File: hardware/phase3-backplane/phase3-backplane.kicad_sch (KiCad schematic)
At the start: 29 parts, among them J1 MANAGER, J10 SLOT0 PWR, J11 SLOT1 PWR, J12 SLOT2 PWR, J13 SLOT3 PWR, J14 SLOT4 PWR, J15 SLOT5 PWR, J16 SLOT6 PWR, J17 SLOT7 PWR, J2 E-STOP NC (jumper if absent), J20 SLOT0 SIG, J21 SLOT1 SIG, J22 SLOT2 SIG, J23 SLOT3 SIG, J24 SLOT4 SIG, J25 SLOT5 SIG, J26 SLOT6 SIG, J27 SLOT7 SIG, J30 VBUS+ LUG M6, J31 RETURN LUG M6, U1 INA228

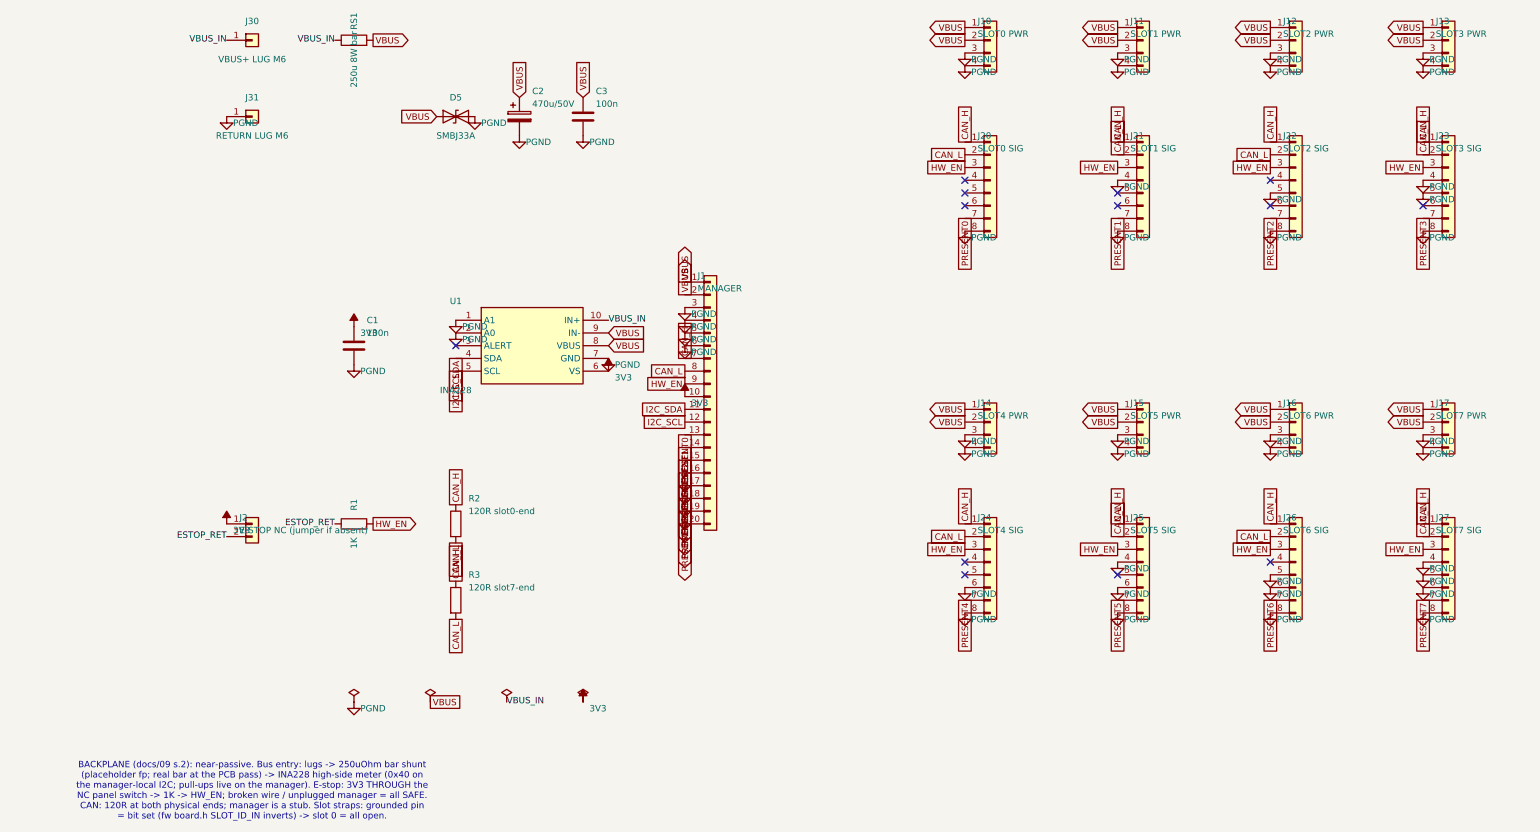
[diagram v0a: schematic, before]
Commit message: Apply China-sourcing engineering changes across all boards + mechanical frame
All datasheet-verified before application (details hardware/SOURCING.md sF):
- TMUX1101 -> TS5A3166DBVR (LCSC availability; ts5a3166.pdf: pin POSITIONS
  identical - 1=NO 2=COM 3=GND 4=IN 5=V+; VIH 2.4V ok from 3.3V GPIO)
- TLV7011 DBVR -> DCKR: tlv7022.pdf shows DBV/DCK share one pinout, so
  footprint-only (SOT-353_SC-70-5); SOT-23-5 stock in China is nearly gone
- crystal load caps 10p -> 18p, both phases (CL=12pF China crystals; the
  HANDOVER-blessed alternative to hunting CL=8pF parts)
- Phase-1 inductor -> MWSA1707S-100MT (JLCPCB-verified 16.5A Isat/10.5A
  Irms vs 12A/8A required); value strings now dual-source Sunlord/Coilcraft
- module slot power + P2 output -> XT60PW-M (2-pin), backplane slots ->
  XT60PW-F; bus shunt -> 2x BVS-M-R0005 parallel (the exact-net checker
  caught RS1/RS2 placed one pin-span apart merging VBUS_IN into VBUS)
- 470u bulk -> THT radial D10; output MLCCs 22u -> 10u/50V X7S; buzzer ->
  MLT-8530 (fp placeholder)
All four checker chains green: 137/173/30/80 components.

hardware/MECHANICAL.md (frozen): 30mm slot pitch, P2 130x90 4-layer,
backplane ~330x100 2-layer 2oz, manager 100x80; cost-first stackup (1oz
outer + solder-reinforced bus, 2oz only if the thermal soak demands it);
inductor footprint = SUPERSET pattern accepting Sunlord 1707 AND Coilcraft
XAL1510 so the A/B pair is a pure part swap.

HANDOVER: sub-0.5V mV-accurate output DEFERRED to a future dedicated
linear post-regulator module (user decision 2026-07-18); buck floors
documented (P2 0.7V @30V bus, P1 0.5V).

Co-Authored-By: Claude Fable 5 <noreply@anthropic.com>
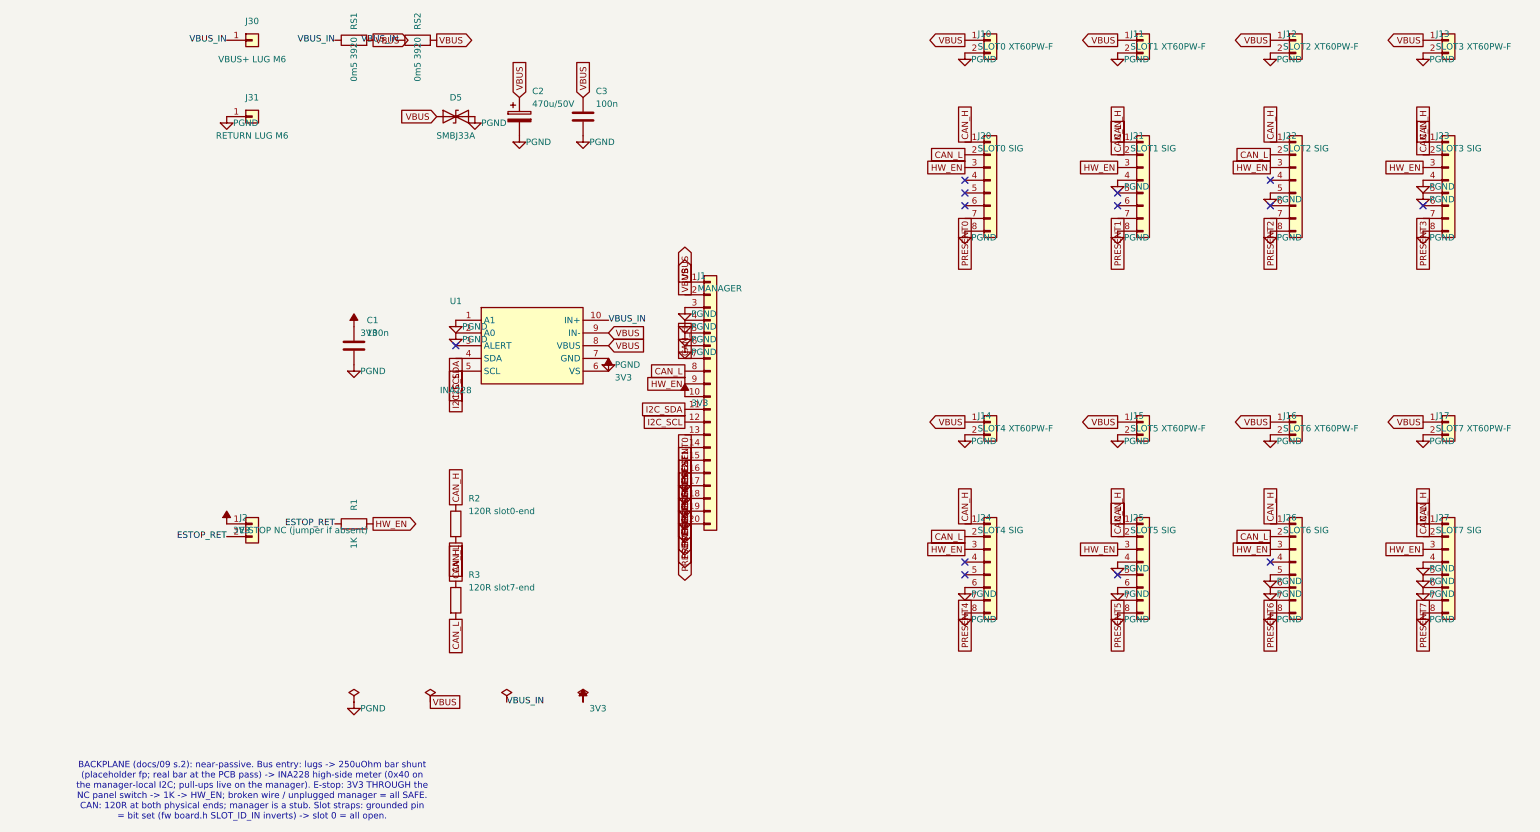
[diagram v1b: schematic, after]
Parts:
- removed J10: SLOT0 PWR, Connector_PinHeader_2.54mm:PinHeader_1x04_P2.54mm_Vertical, symbol Connector_Generic:Conn_01x04
- removed J11: SLOT1 PWR, Connector_PinHeader_2.54mm:PinHeader_1x04_P2.54mm_Vertical, symbol Connector_Generic:Conn_01x04
- removed J12: SLOT2 PWR, Connector_PinHeader_2.54mm:PinHeader_1x04_P2.54mm_Vertical, symbol Connector_Generic:Conn_01x04
- removed J13: SLOT3 PWR, Connector_PinHeader_2.54mm:PinHeader_1x04_P2.54mm_Vertical, symbol Connector_Generic:Conn_01x04
- removed J14: SLOT4 PWR, Connector_PinHeader_2.54mm:PinHeader_1x04_P2.54mm_Vertical, symbol Connector_Generic:Conn_01x04
- removed J15: SLOT5 PWR, Connector_PinHeader_2.54mm:PinHeader_1x04_P2.54mm_Vertical, symbol Connector_Generic:Conn_01x04
- removed J16: SLOT6 PWR, Connector_PinHeader_2.54mm:PinHeader_1x04_P2.54mm_Vertical, symbol Connector_Generic:Conn_01x04
- removed J17: SLOT7 PWR, Connector_PinHeader_2.54mm:PinHeader_1x04_P2.54mm_Vertical, symbol Connector_Generic:Conn_01x04
- added J10: SLOT0 XT60PW-F, Connector_PinHeader_2.54mm:PinHeader_1x02_P2.54mm_Vertical, symbol Connector_Generic:Conn_01x02
- added J11: SLOT1 XT60PW-F, Connector_PinHeader_2.54mm:PinHeader_1x02_P2.54mm_Vertical, symbol Connector_Generic:Conn_01x02
- added J12: SLOT2 XT60PW-F, Connector_PinHeader_2.54mm:PinHeader_1x02_P2.54mm_Vertical, symbol Connector_Generic:Conn_01x02
- added J13: SLOT3 XT60PW-F, Connector_PinHeader_2.54mm:PinHeader_1x02_P2.54mm_Vertical, symbol Connector_Generic:Conn_01x02
- added J14: SLOT4 XT60PW-F, Connector_PinHeader_2.54mm:PinHeader_1x02_P2.54mm_Vertical, symbol Connector_Generic:Conn_01x02
- added J15: SLOT5 XT60PW-F, Connector_PinHeader_2.54mm:PinHeader_1x02_P2.54mm_Vertical, symbol Connector_Generic:Conn_01x02
- added J16: SLOT6 XT60PW-F, Connector_PinHeader_2.54mm:PinHeader_1x02_P2.54mm_Vertical, symbol Connector_Generic:Conn_01x02
- added J17: SLOT7 XT60PW-F, Connector_PinHeader_2.54mm:PinHeader_1x02_P2.54mm_Vertical, symbol Connector_Generic:Conn_01x02
- added RS2: 0m5 3920, Resistor_SMD:R_2512_6332Metric, symbol Device:R
- RS1: value 250u 8W bar -> 0m5 3920
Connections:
- net PGND: now also J10.2 (Pin_2), J11.2 (Pin_2), J12.2 (Pin_2), J13.2 (Pin_2), J14.2 (Pin_2), J15.2 (Pin_2), J16.2 (Pin_2), J17.2 (Pin_2)
- net VBUS: now also J10.1 (Pin_1), J11.1 (Pin_1), J12.1 (Pin_1), J13.1 (Pin_1), J14.1 (Pin_1), J15.1 (Pin_1), J16.1 (Pin_1), J17.1 (Pin_1), RS2.2
- net VBUS_IN: now also RS2.1

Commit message: Footprint pass: China-part land patterns generated, placeholders retired
build_fplib.py sourcing_footprints() - geometry vetted from LCSC/EasyEDA
library pulls (easyeda2kicad), encoded in code like the PowerFET precedent
so regeneration needs no network:
- XT60PW-M / XT60PW-F: power pins 3.8mm pads / 2.9-2.8mm drills @ 7.2mm
  pitch + 0.6x1.6 retention slots. The -F library pull had the RETENTION
  LEGS numbered as pads 1,2 - power pads renumbered to 1,2 to match the -M
  and the Conn_01x02 symbol (a trap no netlist check would ever catch)
- L_1707_XAL1510: SUPERSET pad 5.39x13.2 @ +/-6.405 covering Sunlord
  MWSA1707S (3.5x12.8 @ 7.35) and Coilcraft XAL1510 (3.18x13.2 @ 5.3) -
  the A/B thermal pair and the P1 10uH are pure part swaps
- R3920_BVS bar shunt, MLT-8530 buzzer (edge pads paired 1,1/2,2)
Generators swapped off placeholders (P1 L1, P2 L1/L3/J1/J4, backplane
slots+RS pair, manager buzzer); all four chains green (137/173/30/80).

MECHANICAL.md: insertion geometry corrected to server-PSU style (vertical
rear backplane, modules slide horizontally; XT60 height stagger = power-
first mating). HARD GATE added: XT60 +/- pad mating is ASSUMED until a
mated pair is buzzed out on arrival - required before gerber submission.

Co-Authored-By: Claude Fable 5 <noreply@anthropic.com>
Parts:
- J10, J11, J12, J13, J14, J15, J16, J17: footprint Connector_PinHeader_2.54mm:PinHeader_1x02_P2.54mm_Vertical -> labbench:XT60PW-F
- RS1, RS2: footprint Resistor_SMD:R_2512_6332Metric -> labbench:R3920_BVS
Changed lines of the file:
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@@
     (property "Reference" "RS1" (at 45.72 36.83 0) (effects (font (size 1.27 1.27))))
     (property "Value" "0m5 3920" (at 45.72 44.45 0) (effects (font (size 1.27 1.27))))
-    (property "Footprint" "Resistor_SMD:R_2512_6332Metric" (at 45.72 40.64 0) (effects (font (size 1.27 1.27)) hide))
+    (property "Footprint" "labbench:R3920_BVS" (at 45.72 40.64 0) (effects (font (size 1.27 1.27)) hide))
     (property "Datasheet" "~" (at 45.72 40.64 0) (effects (font (size 1.27 1.27)) hide))
     (pin "1")
@@
     (property "Reference" "RS2" (at 58.42 36.83 0) (effects (font (size 1.27 1.27))))
     (property "Value" "0m5 3920" (at 58.42 44.45 0) (effects (font (size 1.27 1.27))))
-    (property "Footprint" "Resistor_SMD:R_2512_6332Metric" (at 58.42 40.64 0) (effects (font (size 1.27 1.27)) hide))
+    (property "Footprint" "labbench:R3920_BVS" (at 58.42 40.64 0) (effects (font (size 1.27 1.27)) hide))
     (property "Datasheet" "~" (at 58.42 40.64 0) (effects (font (size 1.27 1.27)) hide))
     (pin "1")
@@
     (property "Reference" "J10" (at 170.17999999999998 39.37 0) (effects (font (size 1.27 1.27)) (justify left)))
     (property "Value" "SLOT0 XT60PW-F" (at 170.17999999999998 41.910000000000004 0) (effects (font (size 1.27 1.27)) (justify left)))
-    (property "Footprint" "Connector_PinHeader_2.54mm:PinHeader_1x02_P2.54mm_Vertical" (at 172.72 40.64 0) (effects (font (size 1.27 1.27)) hide))
+    (property "Footprint" "labbench:XT60PW-F" (at 172.72 40.64 0) (effects (font (size 1.27 1.27)) hide))
     (property "Datasheet" "~" (at 172.72 40.64 0) (effects (font (size 1.27 1.27)) hide))
     (pin "1")
@@
     (property "Reference" "J11" (at 200.66 39.37 0) (effects (font (size 1.27 1.27)) (justify left)))
     (property "Value" "SLOT1 XT60PW-F" (at 200.66 41.910000000000004 0) (effects (font (size 1.27 1.27)) (justify left)))
-    (property "Footprint" "Connector_PinHeader_2.54mm:PinHeader_1x02_P2.54mm_Vertical" (at 203.2 40.64 0) (effects (font (size 1.27 1.27)) hide))
+    (property "Footprint" "labbench:XT60PW-F" (at 203.2 40.64 0) (effects (font (size 1.27 1.27)) hide))
     (property "Datasheet" "~" (at 203.2 40.64 0) (effects (font (size 1.27 1.27)) hide))
     (pin "1")
@@
     (property "Reference" "J12" (at 231.14 39.37 0) (effects (font (size 1.27 1.27)) (justify left)))
     (property "Value" "SLOT2 XT60PW-F" (at 231.14 41.910000000000004 0) (effects (font (size 1.27 1.27)) (justify left)))
-    (property "Footprint" "Connector_PinHeader_2.54mm:PinHeader_1x02_P2.54mm_Vertical" (at 233.68 40.64 0) (effects (font (size 1.27 1.27)) hide))
+    (property "Footprint" "labbench:XT60PW-F" (at 233.68 40.64 0) (effects (font (size 1.27 1.27)) hide))
     (property "Datasheet" "~" (at 233.68 40.64 0) (effects (font (size 1.27 1.27)) hide))
     (pin "1")
@@
     (property "Reference" "J13" (at 261.62 39.37 0) (effects (font (size 1.27 1.27)) (justify left)))
     (property "Value" "SLOT3 XT60PW-F" (at 261.62 41.910000000000004 0) (effects (font (size 1.27 1.27)) (justify left)))
-    (property "Footprint" "Connector_PinHeader_2.54mm:PinHeader_1x02_P2.54mm_Vertical" (at 264.15999999999997 40.64 0) (effects (font (size 1.27 1.27)) hide))
+    (property "Footprint" "labbench:XT60PW-F" (at 264.15999999999997 40.64 0) (effects (font (size 1.27 1.27)) hide))
     (property "Datasheet" "~" (at 264.15999999999997 40.64 0) (effects (font (size 1.27 1.27)) hide))
     (pin "1")
@@
     (property "Reference" "J14" (at 170.17999999999998 115.57000000000001 0) (effects (font (size 1.27 1.27)) (justify left)))
     (property "Value" "SLOT4 XT60PW-F" (at 170.17999999999998 118.11 0) (effects (font (size 1.27 1.27)) (justify left)))
-    (property "Footprint" "Connector_PinHeader_2.54mm:PinHeader_1x02_P2.54mm_Vertical" (at 172.72 116.84 0) (effects (font (size 1.27 1.27)) hide))
+    (property "Footprint" "labbench:XT60PW-F" (at 172.72 116.84 0) (effects (font (size 1.27 1.27)) hide))
     (property "Datasheet" "~" (at 172.72 116.84 0) (effects (font (size 1.27 1.27)) hide))
     (pin "1")
@@
     (property "Reference" "J15" (at 200.66 115.57000000000001 0) (effects (font (size 1.27 1.27)) (justify left)))
     (property "Value" "SLOT5 XT60PW-F" (at 200.66 118.11 0) (effects (font (size 1.27 1.27)) (justify left)))
-    (property "Footprint" "Connector_PinHeader_2.54mm:PinHeader_1x02_P2.54mm_Vertical" (at 203.2 116.84 0) (effects (font (size 1.27 1.27)) hide))
+    (property "Footprint" "labbench:XT60PW-F" (at 203.2 116.84 0) (effects (font (size 1.27 1.27)) hide))
     (property "Datasheet" "~" (at 203.2 116.84 0) (effects (font (size 1.27 1.27)) hide))
     (pin "1")
@@
     (property "Reference" "J16" (at 231.14 115.57000000000001 0) (effects (font (size 1.27 1.27)) (justify left)))
     (property "Value" "SLOT6 XT60PW-F" (at 231.14 118.11 0) (effects (font (size 1.27 1.27)) (justify left)))
-    (property "Footprint" "Connector_PinHeader_2.54mm:PinHeader_1x02_P2.54mm_Vertical" (at 233.68 116.84 0) (effects (font (size 1.27 1.27)) hide))
+    (property "Footprint" "labbench:XT60PW-F" (at 233.68 116.84 0) (effects (font (size 1.27 1.27)) hide))
     (property "Datasheet" "~" (at 233.68 116.84 0) (effects (font (size 1.27 1.27)) hide))
     (pin "1")
@@
     (property "Reference" "J17" (at 261.62 115.57000000000001 0) (effects (font (size 1.27 1.27)) (justify left)))
     (property "Value" "SLOT7 XT60PW-F" (at 261.62 118.11 0) (effects (font (size 1.27 1.27)) (justify left)))
-    (property "Footprint" "Connector_PinHeader_2.54mm:PinHeader_1x02_P2.54mm_Vertical" (at 264.15999999999997 116.84 0) (effects (font (size 1.27 1.27)) hide))
+    (property "Footprint" "labbench:XT60PW-F" (at 264.15999999999997 116.84 0) (effects (font (size 1.27 1.27)) hide))
     (property "Datasheet" "~" (at 264.15999999999997 116.84 0) (effects (font (size 1.27 1.27)) hide))
     (pin "1")
